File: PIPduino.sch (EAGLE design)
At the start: 41 parts, among them IC1 ATmega328P\, IC2 SPX1117, J1 ISP/SPI

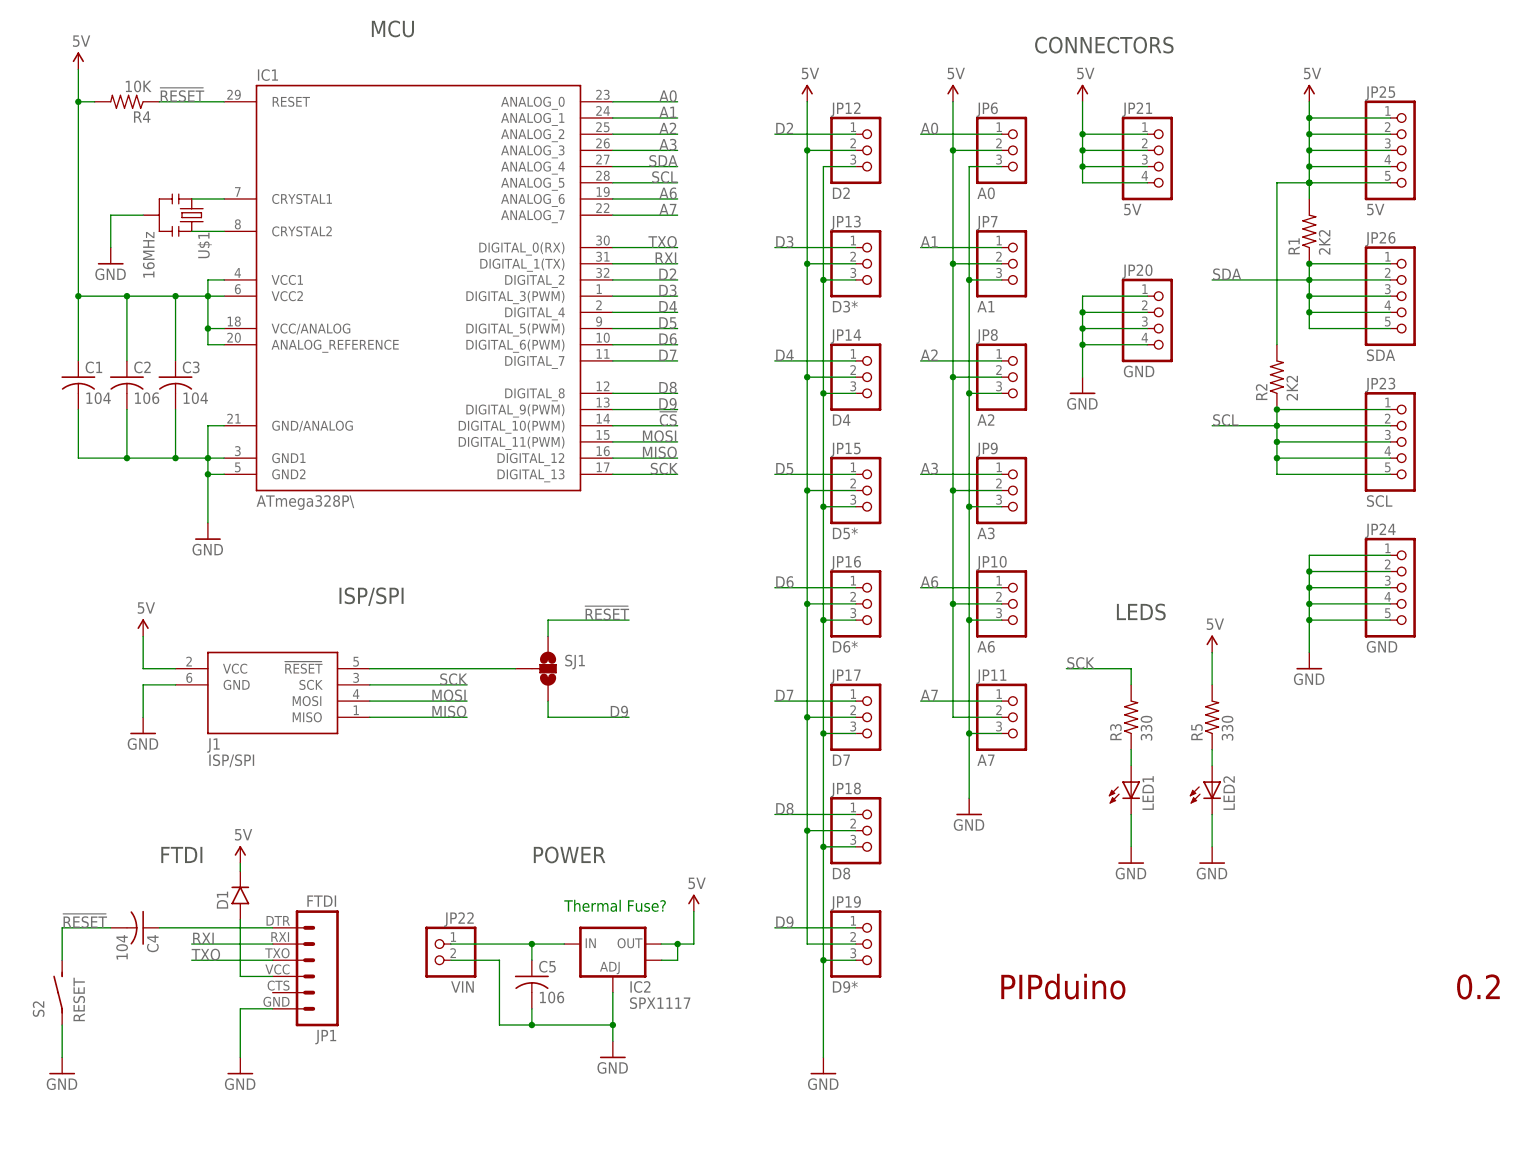
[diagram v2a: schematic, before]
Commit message: Removed top 5V polygon, star pattern power, 106's on analog, 104 on aref, larger power traces, removed polygons on top mounting holes
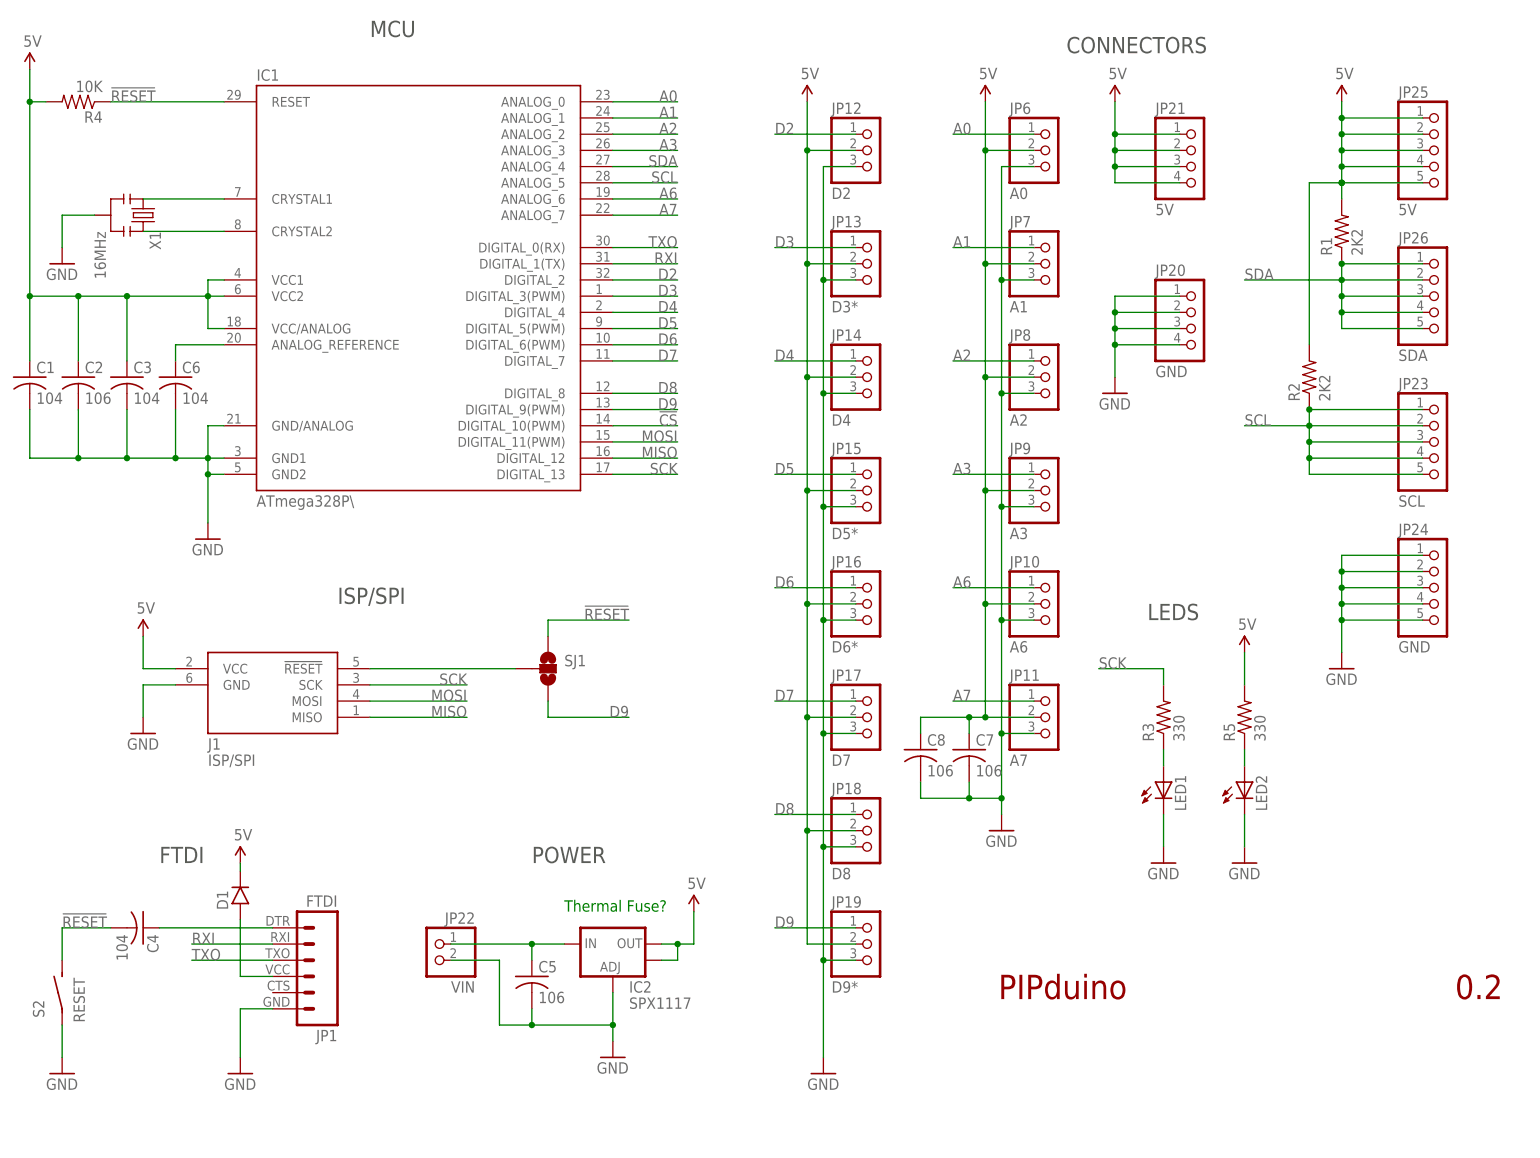
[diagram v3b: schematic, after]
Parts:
- removed U$1: 16MHz, bt_crystal:RESONATOR_CSTCE_V_C
- added C6: 104, rcl:C-USC0603
- added C7, C8: 106, rcl:C-USC1206
- added X1: 16MHz, bt_crystal:RESONATOR_CSTCE_V_C
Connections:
- new net N$6: C6.1, IC1.ANALOG_REFERENCE
- net 5V: now also C7.1, C8.1; no longer IC1.ANALOG_REFERENCE
- net GND: now also C6.2, C7.2, C8.2, X1.GND; no longer U$1.GND
- net N$13: now also X1.X2; no longer U$1.X2
- net N$8: now also X1.X1; no longer U$1.X1
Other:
- moved on the sheet: C1, C2, C3, JP10, JP11, JP20, JP21, JP23, JP24, JP25, JP26, JP6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

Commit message: Final LDO regulator selection, rearrangement, silk updates, fixed missing D10
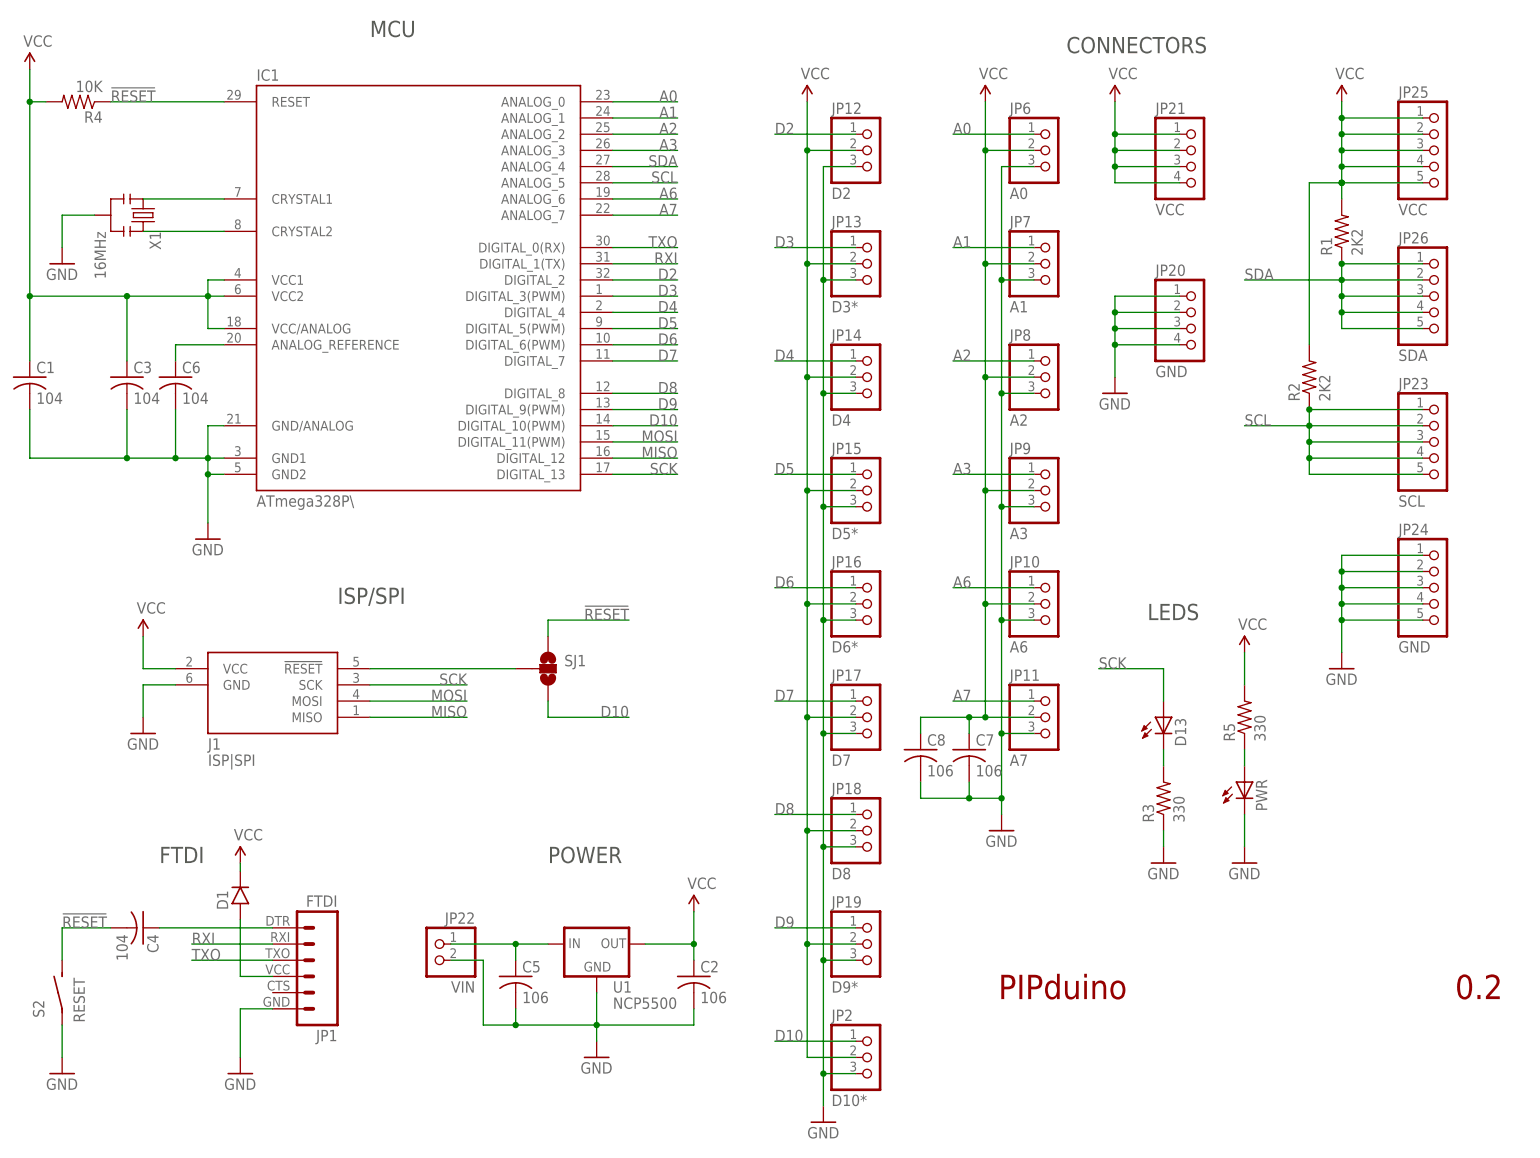
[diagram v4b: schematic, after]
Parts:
- removed IC2: SPX1117, SparkFun:V_REG_LM1117SOT223
- removed LED1: (no value), bt_opto:LED3MM
- added D13: (no value), bt_opto:LED3MM
- added JP2: D10*, pinhead-2:PINHD-1X03_2.54-S
- added U1: NCP5500, bt_regulator:NCP5500
- J1: value ISP/SPI -> ISP|SPI
- JP21, JP25: value 5V -> VCC
- renumbered LED2 to PWR
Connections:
- removed net !CS: IC1.DIGITAL_10(PWM)
- removed net 5V: C1.1, C2.1, C3.1, C7.1, C8.1, D1.C, IC1.VCC/ANALOG, IC1.VCC1, IC1.VCC2, IC2.OUT, IC2.OUT@1, J1.VCC, JP10.2, JP11.2, JP12.2, JP13.2, JP14.2, JP15.2, JP16.2, JP17.2, JP18.2, JP19.2, JP21.1, JP21.2, JP21.3, JP21.4, JP25.1, JP25.2, JP25.3, JP25.4, JP25.5, JP6.2, JP7.2, JP8.2, JP9.2, R1.2, R2.2, R4.2, R5.2
- new net D10: IC1.DIGITAL_10(PWM), JP2.1, SJ1.3
- new net VCC: C1.1, C2.1, C3.1, C7.1, C8.1, D1.C, IC1.VCC/ANALOG, IC1.VCC1, IC1.VCC2, J1.VCC, JP10.2, JP11.2, JP12.2, JP13.2, JP14.2, JP15.2, JP16.2, JP17.2, JP18.2, JP19.2, JP2.2, JP21.1, JP21.2, JP21.3, JP21.4, JP25.1, JP25.2, JP25.3, JP25.4, JP25.5, JP6.2, JP7.2, JP8.2, JP9.2, R1.2, R2.2, R4.2, R5.2, U1.VOUT
- net D9: no longer SJ1.3
- net GND: now also JP2.3, R3.1, U1.GND; no longer IC2.ADJ, LED1.C
- net N$1: now also D13.C, R3.2; no longer LED1.A, R3.1
- net N$2: now also U1.VIN; no longer IC2.IN
- net SCK: now also D13.A; no longer R3.2
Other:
- note removed: "Thermal Fuse?"
- moved on the sheet: C2, C5, R3

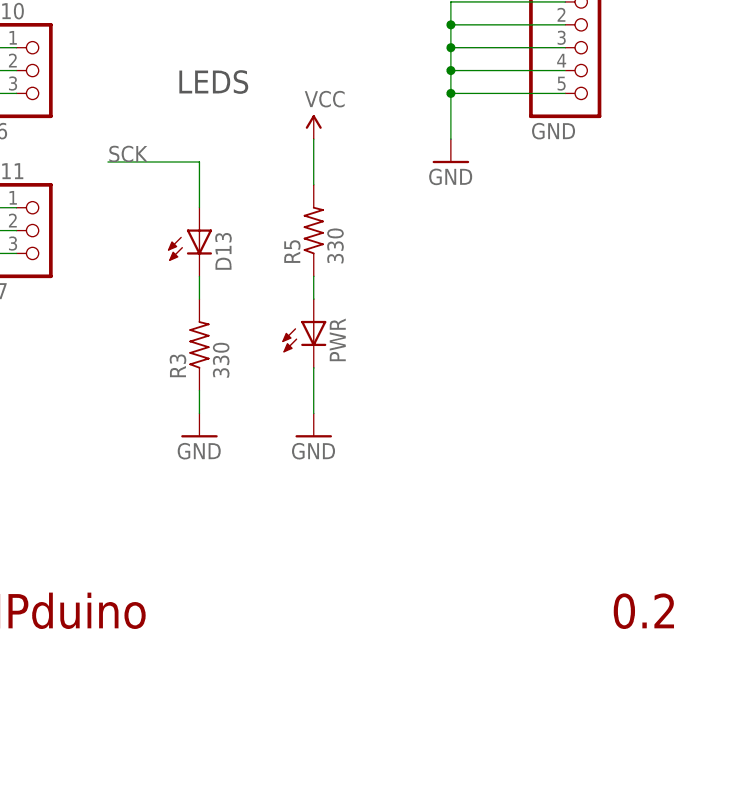
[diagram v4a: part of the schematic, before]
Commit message: Improved thermal design, minor silk fixes, revised LED design for 330 ohm reflow DFM
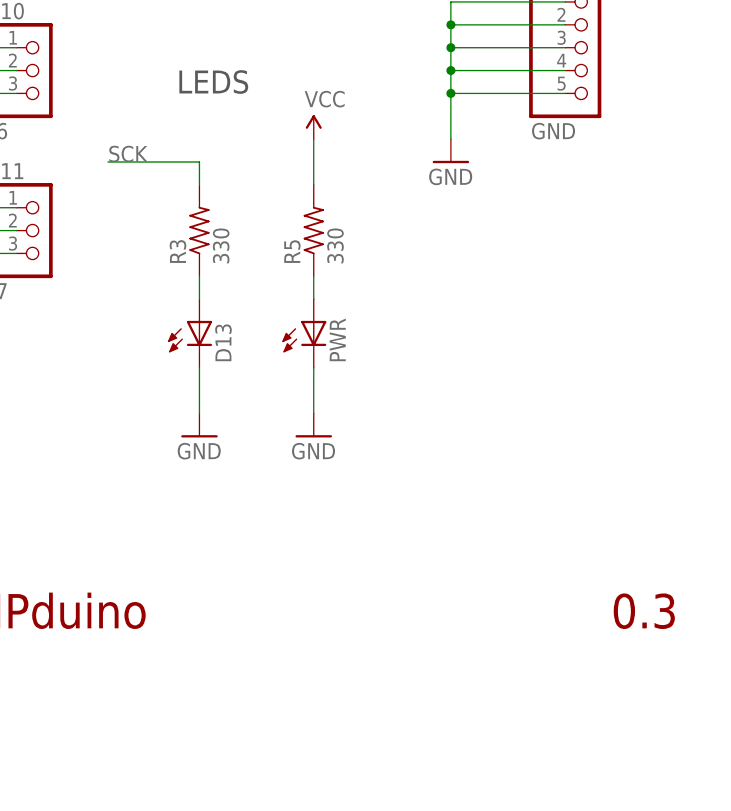
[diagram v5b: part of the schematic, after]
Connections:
- net GND: now also D13.C; no longer R3.1
- net N$1: now also D13.A, R3.1; no longer D13.C, R3.2
- net SCK: now also R3.2; no longer D13.A
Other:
- note added: "0.3"
- note removed: "0.2"
- moved on the sheet: D13, R3
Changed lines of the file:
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@@
 <text x="182.88" y="83.82" size="2.54" layer="97">LEDS</text>
 <text x="159.512" y="24.384" size="3.81" layer="94">PIPduino</text>
-<text x="231.14" y="24.384" size="3.81" layer="94">0.2</text>
+<text x="231.14" y="24.384" size="3.81" layer="94">0.3</text>
 </plain>
 <instances>
@@
 <instance part="C5" gate="G$1" x="83.82" y="27.94"/>
 <instance part="SJ1" gate="G$1" x="88.9" y="76.2"/>
-<instance part="R3" gate="G$1" x="185.42" y="55.88" rot="R90"/>
-<instance part="D13" gate="G$1" x="185.42" y="68.58"/>
+<instance part="R3" gate="G$1" x="185.42" y="68.58" rot="R90"/>
+<instance part="D13" gate="G$1" x="185.42" y="58.42"/>
 <instance part="PWR" gate="G$1" x="198.12" y="58.42"/>
 <instance part="R5" gate="G$1" x="198.12" y="68.58" rot="R90"/>
@@
 <wire x1="185.42" y1="76.2" x2="175.26" y2="76.2" width="0.1524" layer="91"/>
 <label x="175.26" y="76.2" size="1.778" layer="95"/>
-<pinref part="D13" gate="G$1" pin="A"/>
-<wire x1="185.42" y1="71.12" x2="185.42" y2="76.2" width="0.1524" layer="91"/>
+<pinref part="R3" gate="G$1" pin="2"/>
+<wire x1="185.42" y1="73.66" x2="185.42" y2="76.2" width="0.1524" layer="91"/>
 </segment>
 </net>
@@
 <segment>
 <pinref part="GND10" gate="1" pin="GND"/>
-<pinref part="R3" gate="G$1" pin="1"/>
-<wire x1="185.42" y1="50.8" x2="185.42" y2="48.26" width="0.1524" layer="91"/>
+<pinref part="D13" gate="G$1" pin="C"/>
+<wire x1="185.42" y1="48.26" x2="185.42" y2="53.34" width="0.1524" layer="91"/>
 </segment>
 </net>
@@
 <wire x1="38.1" y1="127" x2="30.48" y2="127" width="0.1524" layer="91"/>
 <wire x1="30.48" y1="127" x2="30.48" y2="124.46" width="0.1524" layer="91"/>
-</segment>
-</net>
-<net name="N$1" class="0">
-<segment>
-<pinref part="D13" gate="G$1" pin="C"/>
-<pinref part="R3" gate="G$1" pin="2"/>
-<wire x1="185.42" y1="60.96" x2="185.42" y2="63.5" width="0.1524" layer="91"/>
 </segment>
 </net>
@@
 </segment>
 </net>
+<net name="N$1" class="0">
+<segment>
+<pinref part="D13" gate="G$1" pin="A"/>
+<pinref part="R3" gate="G$1" pin="1"/>
+<wire x1="185.42" y1="63.5" x2="185.42" y2="60.96" width="0.1524" layer="91"/>
+</segment>
+</net>
